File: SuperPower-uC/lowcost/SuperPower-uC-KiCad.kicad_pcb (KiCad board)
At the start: 2 copper layers, 83.6 x 28.2 mm, 83 parts, among them J1 Battery connector, J2 Thermistor, J3 USB_B_Micro, J4 Solar in, J5 main pin header right, J6 main pin header left, J7 expander pins nc, J8 expander pins, Q1 2N7002, Q2 2N7002, Q3 S8050, Q4 S8050, Q5 AO3401A, Q6 AO3401A, Q7 2N7002, U1 FS312F-G, U10 FP6291LR, U11 ME6210A33P, U12 ME6210A33P, U13 ESP32-WROOM32, U2 FS8205A, U3 LC709203FQH, U4 TP4056, U5 CH340G, U6 AMS1117-3.3, U7 PCF8563T, U8 XC6206P332MR, U9 TCA6408A, Y1 12MHZ, Y2 32.768KHz

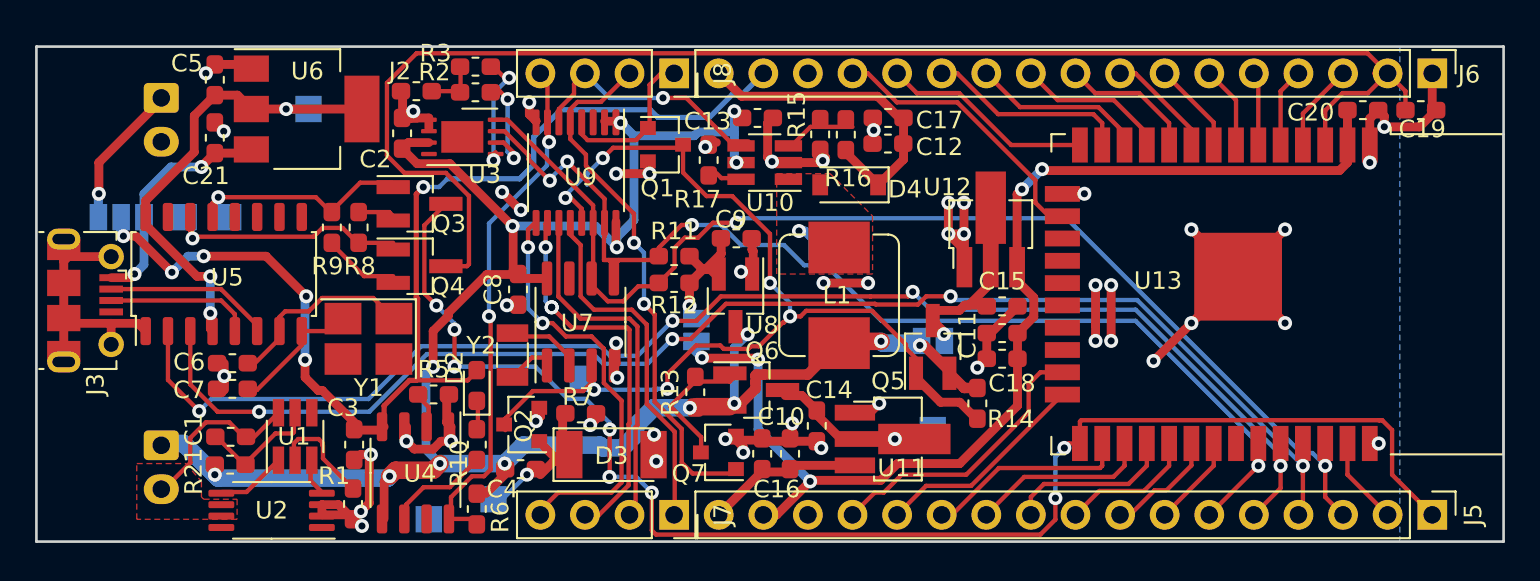
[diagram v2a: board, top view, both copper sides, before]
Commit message: fixed erc errors
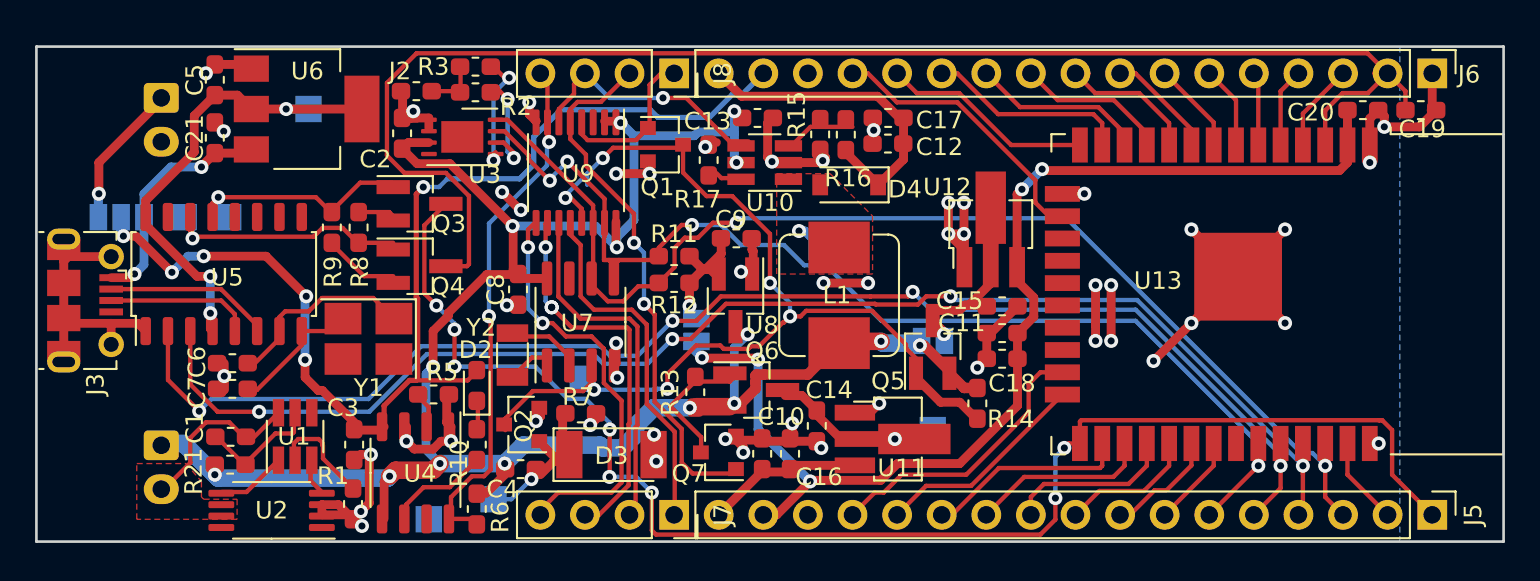
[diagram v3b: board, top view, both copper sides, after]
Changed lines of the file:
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@@
   (page A4)
   (layers
-    (0 F.Cu signal hide)
-    (31 B.Cu signal hide)
+    (0 F.Cu signal)
+    (31 B.Cu signal)
     (32 B.Adhes user hide)
     (33 F.Adhes user hide)
@@
     (35 F.Paste user hide)
     (36 B.SilkS user)
-    (37 F.SilkS user hide)
+    (37 F.SilkS user)
     (38 B.Mask user)
-    (39 F.Mask user hide)
+    (39 F.Mask user)
     (40 Dwgs.User user)
     (41 Cmts.User user)
@@
     (tags "SMD SMT Crystal")
     (attr smd)
-    (fp_text reference Y2 (at 0.5515 -1.778 180) (layer F.SilkS)
+    (fp_text reference Y2 (at 1.5675 -1.778 180) (layer F.SilkS)
       (effects (font (size 1 1) (thickness 0.15)))
     )
@@
     (tags "TSSOP SO")
     (attr smd)
-    (fp_text reference U9 (at 0.249 -0.254 180) (layer F.SilkS)
+    (fp_text reference U9 (at 0.0585 -0.127 180) (layer F.SilkS)
       (effects (font (size 1 1) (thickness 0.15)))
     )
@@
     (tags "resistor handsolder")
     (attr smd)
-    (fp_text reference R11 (at 0 -1.43) (layer F.SilkS)
+    (fp_text reference R11 (at 0 -1.27) (layer F.SilkS)
       (effects (font (size 1 1) (thickness 0.15)))
     )
@@
     (tags "resistor handsolder")
     (attr smd)
-    (fp_text reference R9 (at -2.2085 -0.254 180) (layer F.SilkS)
+    (fp_text reference R9 (at -2.526 0.0635 270) (layer F.SilkS)
       (effects (font (size 1 1) (thickness 0.15)))
     )
@@
     (tags "resistor handsolder")
     (attr smd)
-    (fp_text reference R8 (at 2.2085 -0.0635 180) (layer F.SilkS)
+    (fp_text reference R8 (at 2.526 -0.0635 270) (layer F.SilkS)
       (effects (font (size 1 1) (thickness 0.15)))
     )
@@
     (tags "resistor handsolder")
     (attr smd)
-    (fp_text reference R5 (at 0 -1.43) (layer F.SilkS)
+    (fp_text reference R5 (at 0.494 -1.27) (layer F.SilkS)
       (effects (font (size 1 1) (thickness 0.15)))
     )
@@
     (tags "resistor handsolder")
     (attr smd)
-    (fp_text reference R3 (at 2.272 0.762) (layer F.SilkS)
+    (fp_text reference R3 (at 2.399 0) (layer F.SilkS)
       (effects (font (size 1 1) (thickness 0.15)))
     )
@@
     (tags "resistor handsolder")
     (attr smd)
-    (fp_text reference R2 (at 2.3355 1.143) (layer F.SilkS)
+    (fp_text reference R2 (at -2.3 -0.8255) (layer F.SilkS)
       (effects (font (size 1 1) (thickness 0.15)))
     )
@@
     (tags "resistor handsolder")
     (attr smd)
-    (fp_text reference R1 (at -1.6015 1.0795 180) (layer F.SilkS)
+    (fp_text reference R1 (at -1.6015 1.143 180) (layer F.SilkS)
       (effects (font (size 1 1) (thickness 0.15)))
     )
@@
     (tags SOT-23)
     (attr smd)
-    (fp_text reference Q1 (at -0.4605 2.4765) (layer F.SilkS)
+    (fp_text reference Q1 (at -0.4605 2.413) (layer F.SilkS)
       (effects (font (size 1 1) (thickness 0.15)))
     )
@@
     (tags "LED handsolder")
     (attr smd)
-    (fp_text reference D2 (at 1.016 -1.27 90) (layer F.SilkS)
+    (fp_text reference D2 (at 2.032 -0.0635 180) (layer F.SilkS)
       (effects (font (size 1 1) (thickness 0.15)))
     )
@@
     (tags "capacitor handsolder")
     (attr smd)
-    (fp_text reference C21 (at -2.173 -0.508 180) (layer F.SilkS)
+    (fp_text reference C21 (at -0.014 -1.143 270) (layer F.SilkS)
       (effects (font (size 1 1) (thickness 0.15)))
     )
@@
     (tags "capacitor handsolder")
     (attr smd)
-    (fp_text reference C16 (at -2.018 0.8255 180) (layer F.SilkS)
+    (fp_text reference C16 (at -1.3195 3.2385 180) (layer F.SilkS)
       (effects (font (size 1 1) (thickness 0.15)))
     )
@@
     (tags "capacitor handsolder")
     (attr smd)
-    (fp_text reference C15 (at 0 -1.43) (layer F.SilkS)
+    (fp_text reference C15 (at -2.427 -0.3175) (layer F.SilkS)
       (effects (font (size 1 1) (thickness 0.15)))
     )
@@
     (tags "capacitor handsolder")
     (attr smd)
-    (fp_text reference C11 (at 1.9825 -0.127 90) (layer F.SilkS)
+    (fp_text reference C11 (at 2.3 0.5715 180) (layer F.SilkS)
       (effects (font (size 1 1) (thickness 0.15)))
     )
@@
     (tags "capacitor handsolder")
     (attr smd)
-    (fp_text reference C8 (at 0 -1.43 90) (layer F.SilkS)
+    (fp_text reference C8 (at -0.014 -1.27 90) (layer F.SilkS)
       (effects (font (size 1 1) (thickness 0.15)))
     )
@@
     (tags "capacitor handsolder")
     (attr smd)
-    (fp_text reference C7 (at 2.4625 -0.0635) (layer F.SilkS)
+    (fp_text reference C7 (at 2.018 -0.1905 90) (layer F.SilkS)
       (effects (font (size 1 1) (thickness 0.15)))
     )
@@
     (tags "capacitor handsolder")
     (attr smd)
-    (fp_text reference C6 (at 2.4625 0.0635) (layer F.SilkS)
+    (fp_text reference C6 (at 2.018 0.0635 90) (layer F.SilkS)
       (effects (font (size 1 1) (thickness 0.15)))
     )
@@
     (tags "capacitor handsolder")
     (attr smd)
-    (fp_text reference C5 (at -0.9385 1.5875 180) (layer F.SilkS)
+    (fp_text reference C5 (at 0.014 1.143 270) (layer F.SilkS)
       (effects (font (size 1 1) (thickness 0.15)))
     )
@@
     (tags "capacitor handsolder")
     (attr smd)
-    (fp_text reference C1 (at -2.1095 -0.381 90) (layer F.SilkS)
+    (fp_text reference C1 (at -2.046 -0.508 270) (layer F.SilkS)
       (effects (font (size 1 1) (thickness 0.15)))
     )
@@
   (gr_line (start 101.981 95.123) (end 101.981 123.317) (layer Edge.Cuts) (width 0.15))
   (gr_line (start 185.547 95.123) (end 101.981 95.123) (layer Edge.Cuts) (width 0.15))
-  (via (at 129.921 119.507) (size 0.8) (drill 0.4) (layers F.Cu B.Cu) (net 6))
   (segment (start 110.744 118.832) (end 109.347 120.229) (width 0.25) (layer F.Cu) (net 1))
   (segment (start 110.744 117.4115) (end 110.744 118.832) (width 0.25) (layer F.Cu) (net 1))
@@
   (segment (start 132.334 118.364) (end 132.715 118.364) (width 0.25) (layer F.Cu) (net 6))
   (segment (start 130.429 119.1895) (end 130.429 119.253) (width 0.25) (layer F.Cu) (net 6))
-  (segment (start 130.2385 119.1895) (end 129.921 119.507) (width 0.25) (layer F.Cu) (net 6))
-  (segment (start 130.429 119.1895) (end 130.2385 119.1895) (width 0.25) (layer F.Cu) (net 6))
-  (segment (start 128.524 120.904) (end 129.921 119.507) (width 0.25) (layer B.Cu) (net 6))
-  (segment (start 128.016 120.904) (end 128.524 120.904) (width 0.25) (layer B.Cu) (net 6))
+  (segment (start 129.032 120.904) (end 130.175 119.761) (width 0.25) (layer B.Cu) (net 6))
+  (segment (start 128.016 120.904) (end 129.032 120.904) (width 0.25) (layer B.Cu) (net 6))
+  (segment (start 130.175 119.4435) (end 130.175 119.761) (width 0.25) (layer F.Cu) (net 6))
+  (segment (start 130.429 119.1895) (end 130.175 119.4435) (width 0.25) (layer F.Cu) (net 6))
+  (via (at 130.175 119.761) (size 0.8) (drill 0.4) (layers F.Cu B.Cu) (net 6))
   (via (at 116.205 98.679) (size 0.8) (drill 0.4) (layers F.Cu B.Cu) (net 7))
   (segment (start 114.223 98.679) (end 116.205 98.679) (width 0.508) (layer F.Cu) (net 7))

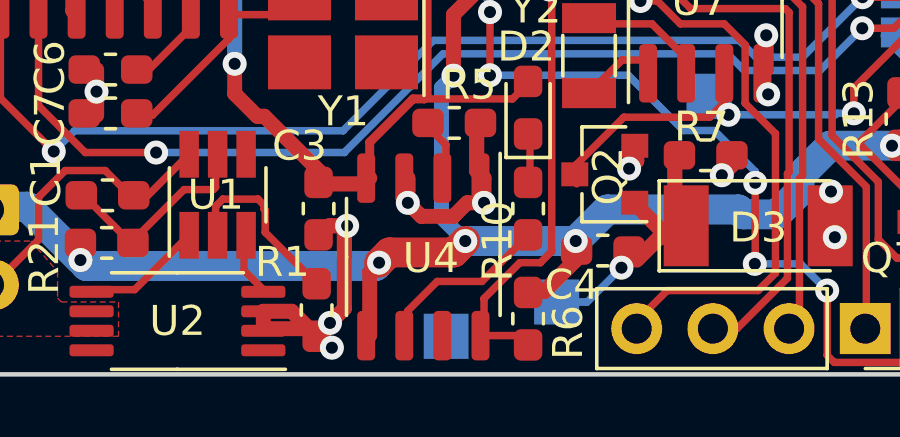
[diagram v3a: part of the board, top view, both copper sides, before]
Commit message: connected tp4
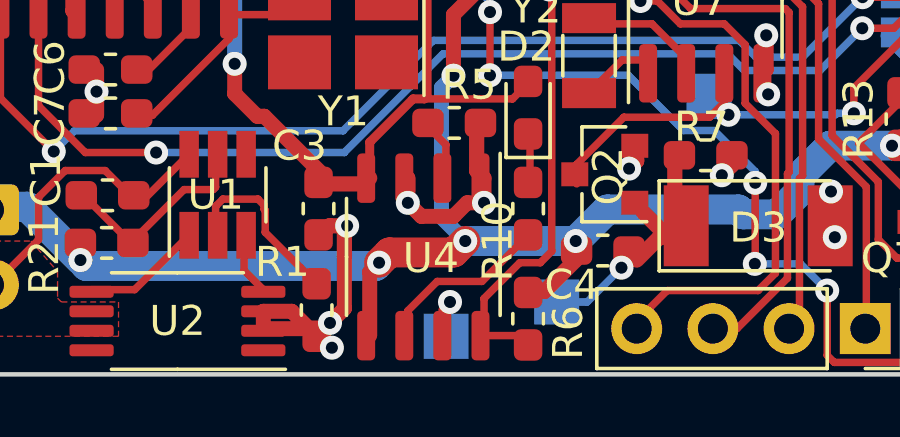
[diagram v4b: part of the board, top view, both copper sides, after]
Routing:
- net Net-(TP4-Pad1): track 0.00 -> 2.42 mm, vias 0 -> 1
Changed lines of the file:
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@@
     (thickness 1.6)
     (drawings 51)
-    (tracks 1023)
+    (tracks 1028)
     (zones 0)
     (modules 83)
@@
   (segment (start 130.2 112.838) (end 129.159 113.879) (width 0.25) (layer F.Cu) (net 83))
   (segment (start 131.064 112.838) (end 130.2 112.838) (width 0.25) (layer F.Cu) (net 83))
+  (via (at 124.46 120.904) (size 0.8) (drill 0.4) (layers F.Cu B.Cu) (net 93))
+  (segment (start 124.206 121.158) (end 124.46 120.904) (width 0.25) (layer F.Cu) (net 93))
+  (segment (start 124.206 122.0265) (end 124.206 121.158) (width 0.25) (layer F.Cu) (net 93))
+  (segment (start 124.46 121.92) (end 124.333 122.047) (width 0.25) (layer B.Cu) (net 93))
+  (segment (start 124.46 120.904) (end 124.46 121.92) (width 0.25) (layer B.Cu) (net 93))
   (segment (start 137.557996 96.647) (end 138.303 96.647) (width 0.25) (layer F.Cu) (net 94))
   (segment (start 136.906 97.298996) (end 137.557996 96.647) (width 0.25) (layer F.Cu) (net 94))

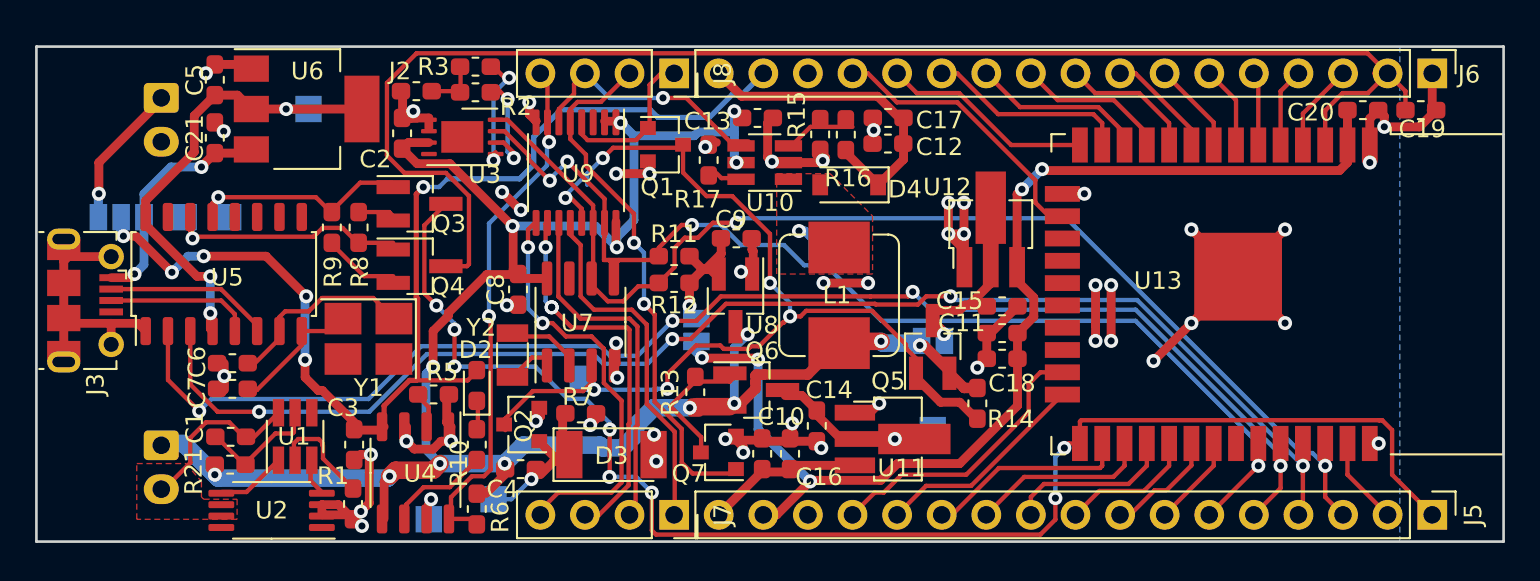
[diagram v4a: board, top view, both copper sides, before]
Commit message: moved connector over to mcu sheet, made some vias smaller ...
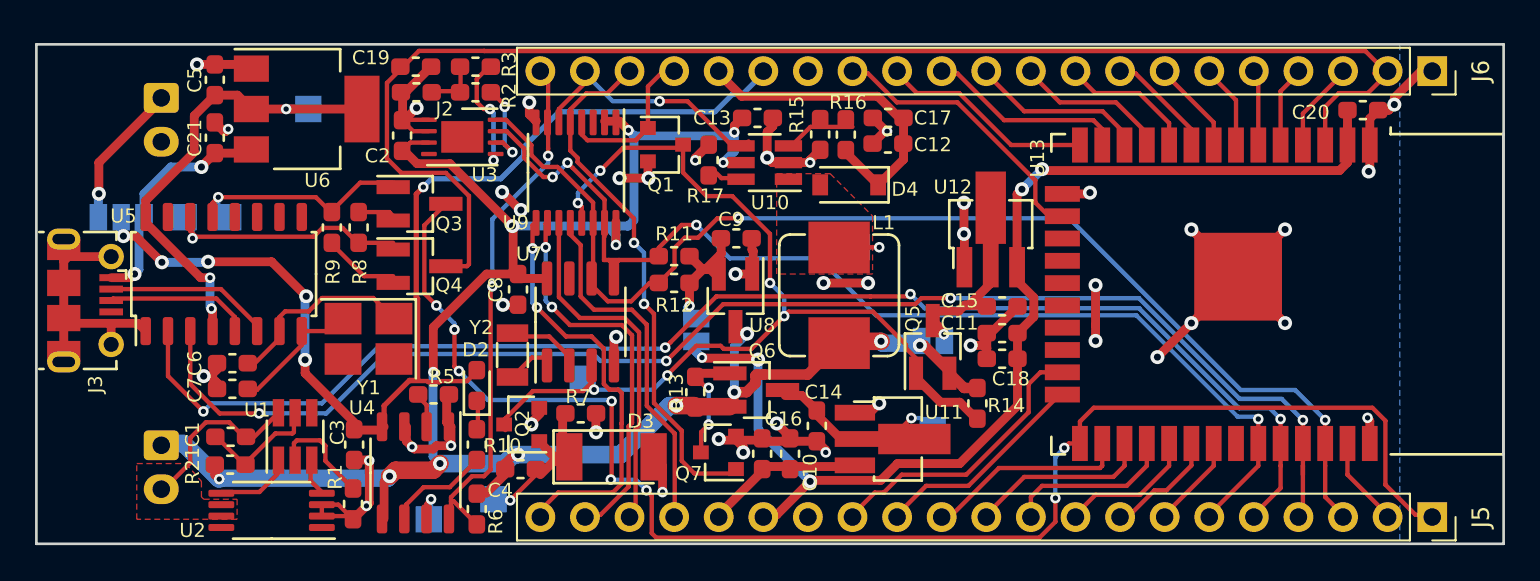
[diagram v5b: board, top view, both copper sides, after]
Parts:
- removed J7: expander pins nc, Connector_PinSocket_2.54mm:PinSocket_1x04_P2.54mm_Vertical
- removed J8: expander pins, Connector_PinSocket_2.54mm:PinSocket_1x04_P2.54mm_Vertical
- J5: value main pin header right -> main pin header fight; footprint Connector_PinHeader_2.54mm:PinHeader_1x17_P2.54mm_Vertical -> Connector_PinSocket_2.54mm:PinSocket_1x21_P2.54mm_Vertical
- J6: footprint Connector_PinHeader_2.54mm:PinHeader_1x17_P2.54mm_Vertical -> Connector_PinSocket_2.54mm:PinSocket_1x21_P2.54mm_Vertical
- moved C19 57.3 mm to (123.6, 96.3)
- moved TP5 2.03 mm to (148.7, 106.6)
- moved J6 0.13 mm to (181.5, 96.5)
- moved C2 0.13 mm to (122.8, 100.2)
- moved D3 0.13 mm to (134.7, 118.5)
- moved J5 0.13 mm to (181.5, 121.9)
- moved J2 0.06 mm to (123.6, 97.7)
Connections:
- Q1 pad 1: /RTC and Cut-Off Module/INT_IO -> INT_IO
- Q7 pad 1: /RTC and Cut-Off Module/3v3V_EN -> 3v3_EN
- R6 pad 2: /Charging Module/CHARGE-DISABLE -> CH_DIS
- U10 pad 4: /RTC and Cut-Off Module/5V_EN -> 5V_EN
- U4 pad 8: /Charging Module/CHARGE-DISABLE -> CH_DIS
- U9 pad 10: Net-(J7-Pad3) -> exp5
- U9 pad 11: Net-(J7-Pad2) -> exp6
- U9 pad 12: Net-(J7-Pad1) -> exp7
- U9 pad 4: /RTC and Cut-Off Module/INT_IO -> INT_IO
- U9 pad 5: /RTC and Cut-Off Module/3v3V_EN -> 3v3_EN
- U9 pad 6: /RTC and Cut-Off Module/5V_EN -> 5V_EN
- U9 pad 7: /Charging Module/CHARGE-DISABLE -> CH_DIS
- U9 pad 9: Net-(J7-Pad4) -> exp4
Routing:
- net CH_DIS: track 0.00 -> 30.6 mm, vias 0 -> 2
- net /RTC and Cut-Off Module/3v3V_EN: track 30.3 -> 0.00 mm, vias 2 -> 0
- net 3v3_EN: track 0.00 -> 30.3 mm, vias 0 -> 2
- net /Charging Module/CHARGE-DISABLE: track 30.3 -> 0.00 mm, vias 2 -> 0
- net Net-(J7-Pad4): track 24.1 -> 0.00 mm, vias 2 -> 0
- net exp4: track 0.00 -> 23.9 mm, vias 0 -> 2
- net exp5: track 0.00 -> 22.4 mm, vias 0 -> 2
- net Net-(J7-Pad3): track 22.3 -> 0.00 mm, vias 3 -> 0
- net exp7: track 0.00 -> 20.6 mm
- net Net-(J7-Pad1): track 20.5 -> 0.00 mm
- net Net-(J7-Pad2): track 20.4 -> 0.00 mm
- net exp6: track 0.00 -> 20.3 mm
- net 5V_EN: track 0.00 -> 14.3 mm, vias 0 -> 1
- net /RTC and Cut-Off Module/5V_EN: track 14.3 -> 0.00 mm, vias 1 -> 0
- net /RTC and Cut-Off Module/INT_IO: track 9.09 -> 0.00 mm
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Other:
- board size 83.6 x 28.2 mm -> 83.6 x 28.4 mm
- rule via_min_size: 0.4 -> 0.6

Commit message: more routing optimisation
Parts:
- moved TP5 1.80 mm to (150.0, 105.3)
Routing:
- net /Charger I/O/GPIO0: track 84.8 -> 94.1 mm, vias 8 -> 6
- net GND: track 125.6 -> 116.4 mm, vias 44 -> 37
- net /Charger I/O/RST: track 81.3 -> 80.6 mm
- net /Charger I/O/VCHARGE: track 64.9 -> 64.4 mm

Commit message: even more optimisation
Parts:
- moved TP2 0.70 mm to (132.6, 113.5)
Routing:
- net /Charging Module/SDA: track 63.0 -> 61.7 mm
- net Net-(R15-Pad1): track 3.56 -> 4.80 mm
- net GND: track 116.4 -> 115.3 mm, vias 37 -> 38
- net /Battery Module/VBAT: track 118.2 -> 119.0 mm
- net /Charger I/O/3v3FTDI: track 26.9 -> 27.7 mm
- net /Charger I/O/VCHARGE: track 64.4 -> 63.8 mm, vias 6 -> 4
- net /Charger I/O/VBUS: track 13.5 -> 12.9 mm
- net Net-(C15-Pad1): track 7.07 -> 6.47 mm
- net CH_DIS: track 30.8 -> 31.3 mm
- net Net-(C1-Pad2): track 9.70 -> 10.2 mm
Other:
- board size 83.6 x 28.4 mm -> 81 x 28.5 mm
